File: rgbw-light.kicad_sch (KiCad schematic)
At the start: 2 parts, among them CN1 1x7

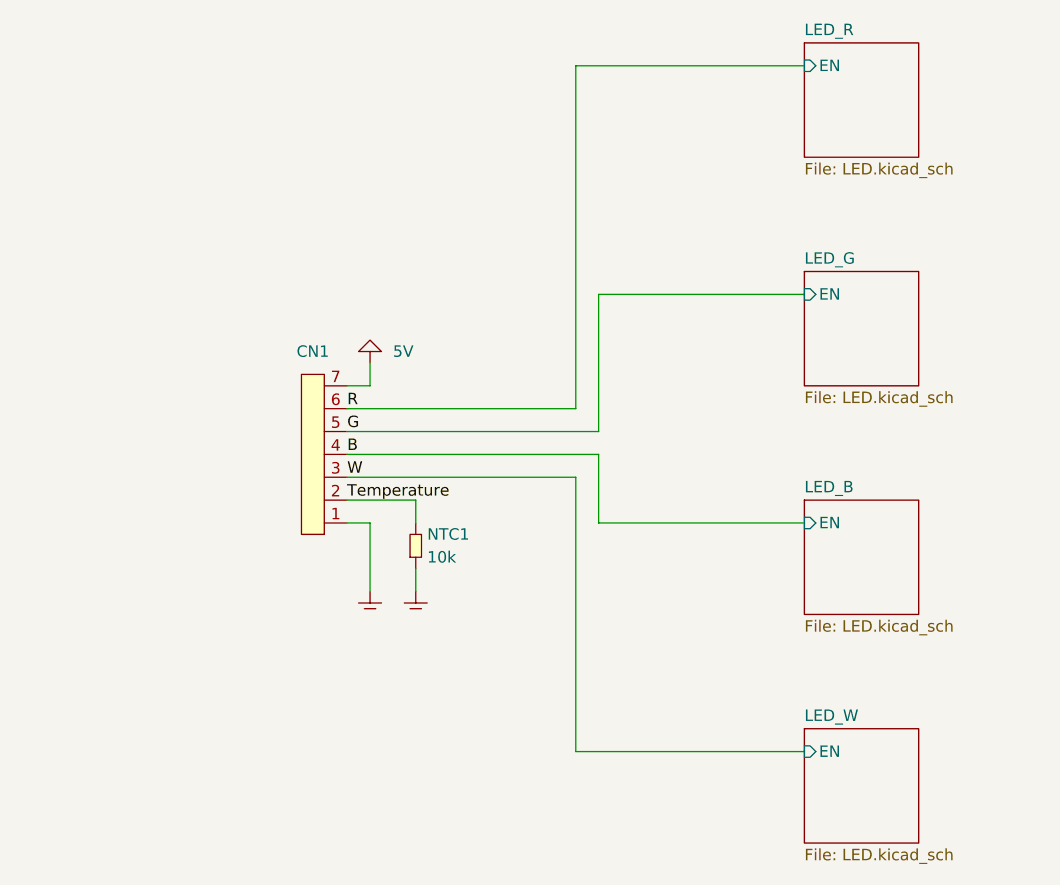
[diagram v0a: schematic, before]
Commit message: changed layout to match d1 mini
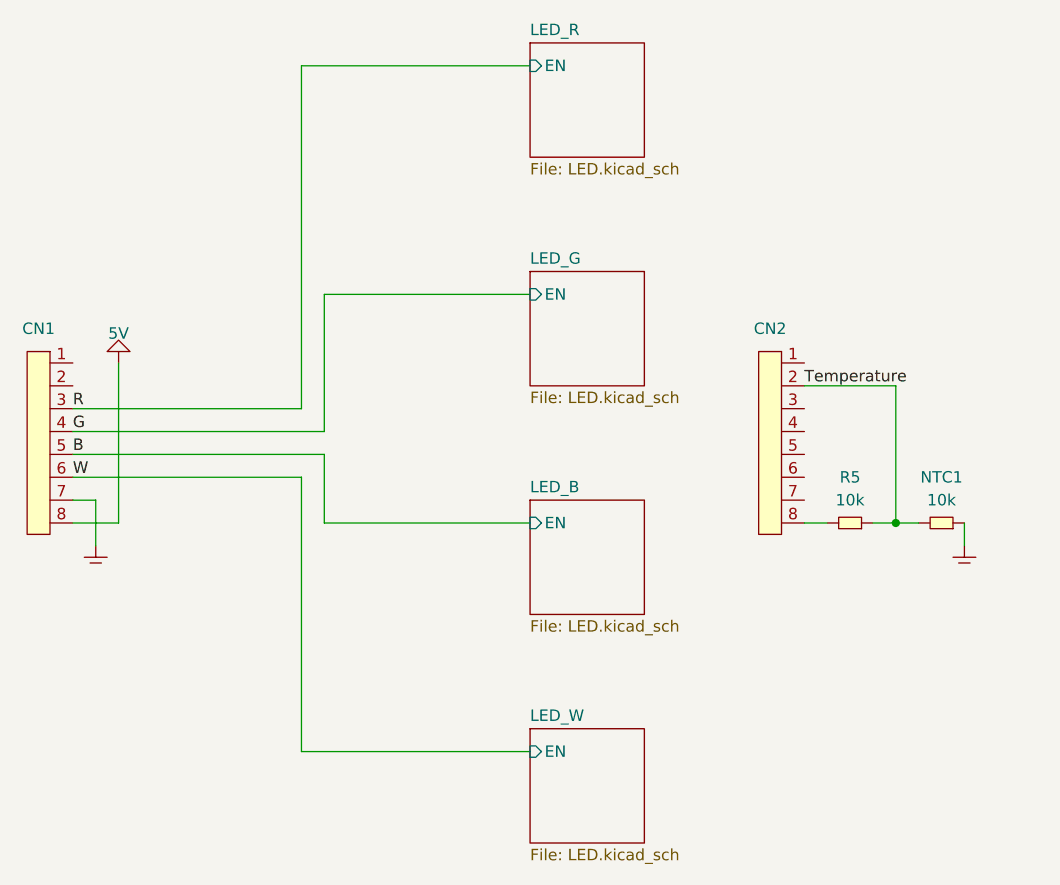
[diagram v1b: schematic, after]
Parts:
- removed CN1: 1x7, pin_headers:1x7, symbol pin_headers:1x7
- added CN1, CN2: 1x8, pin_headers:1x8, symbol pin_headers:1x8
- added R5: 10k, SMT:0603, symbol generic:R
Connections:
- net 5V: now also CN1.8
- net B: now also CN1.5
- net G: now also CN1.4
- net GND: now also CN1.7
- net R: now also CN1.3
- net Temperature: now also CN2.2, R5.1
- net W: now also CN1.6
- new net: CN2.8, R5.2
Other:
- moved on the sheet: NTC1

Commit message: moved blue from FLASH pin to GPIO12
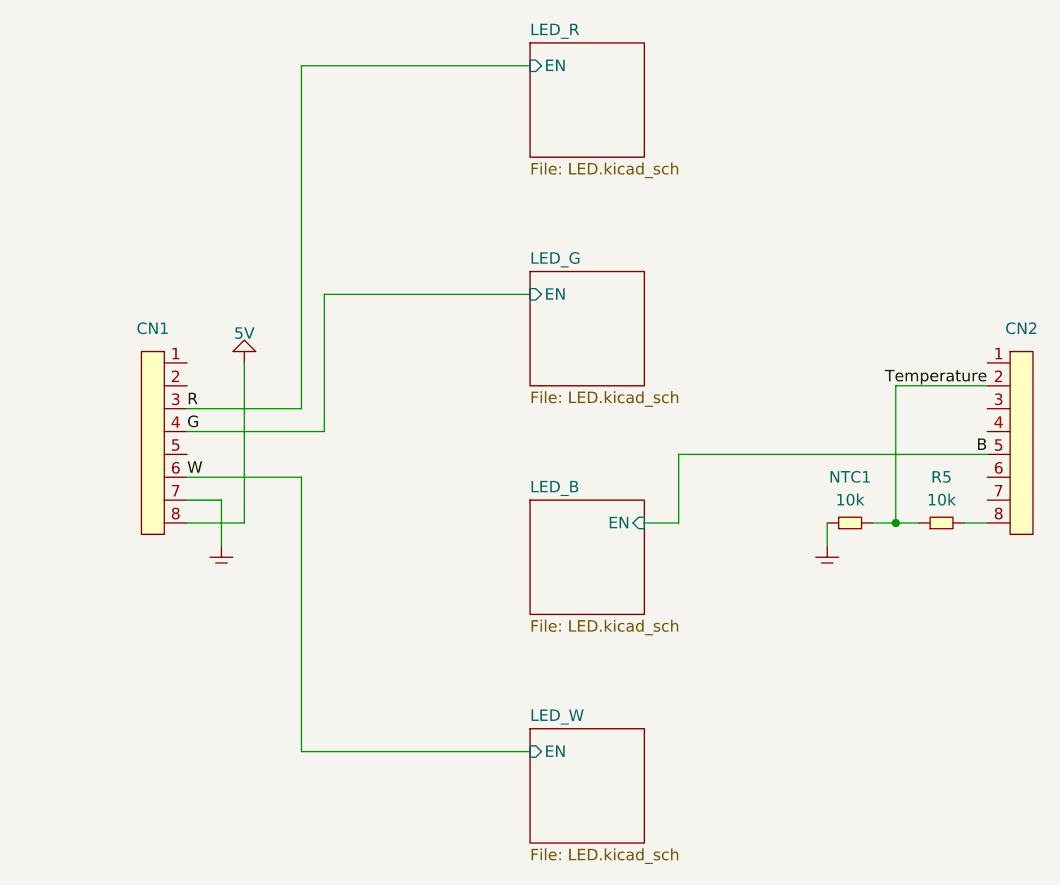
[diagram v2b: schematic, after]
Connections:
- net B: now also CN2.5; no longer CN1.5
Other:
- moved on the sheet: CN1, CN2, NTC1, R5
